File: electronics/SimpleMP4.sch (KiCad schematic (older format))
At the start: 118 parts, among them J1 USB_OTG, J2 DISPLAY, Q1 8050, Q2 SI2305, Q3 SI2305, Q4 8050, Q5 8550, Q6 SI2305, U1 OCP8020, U10 ZLED7012, U2 RK2608, U3 OCP21050TW18A, U4 OCP1240, U5 MT25QL128ABA, U6 K9HCG08U1M-PCB0/PIB0, U7 K4S641632N, U8 TRS_5PIN, U9 MMC/SD_SOCKET, Y1 24MHz

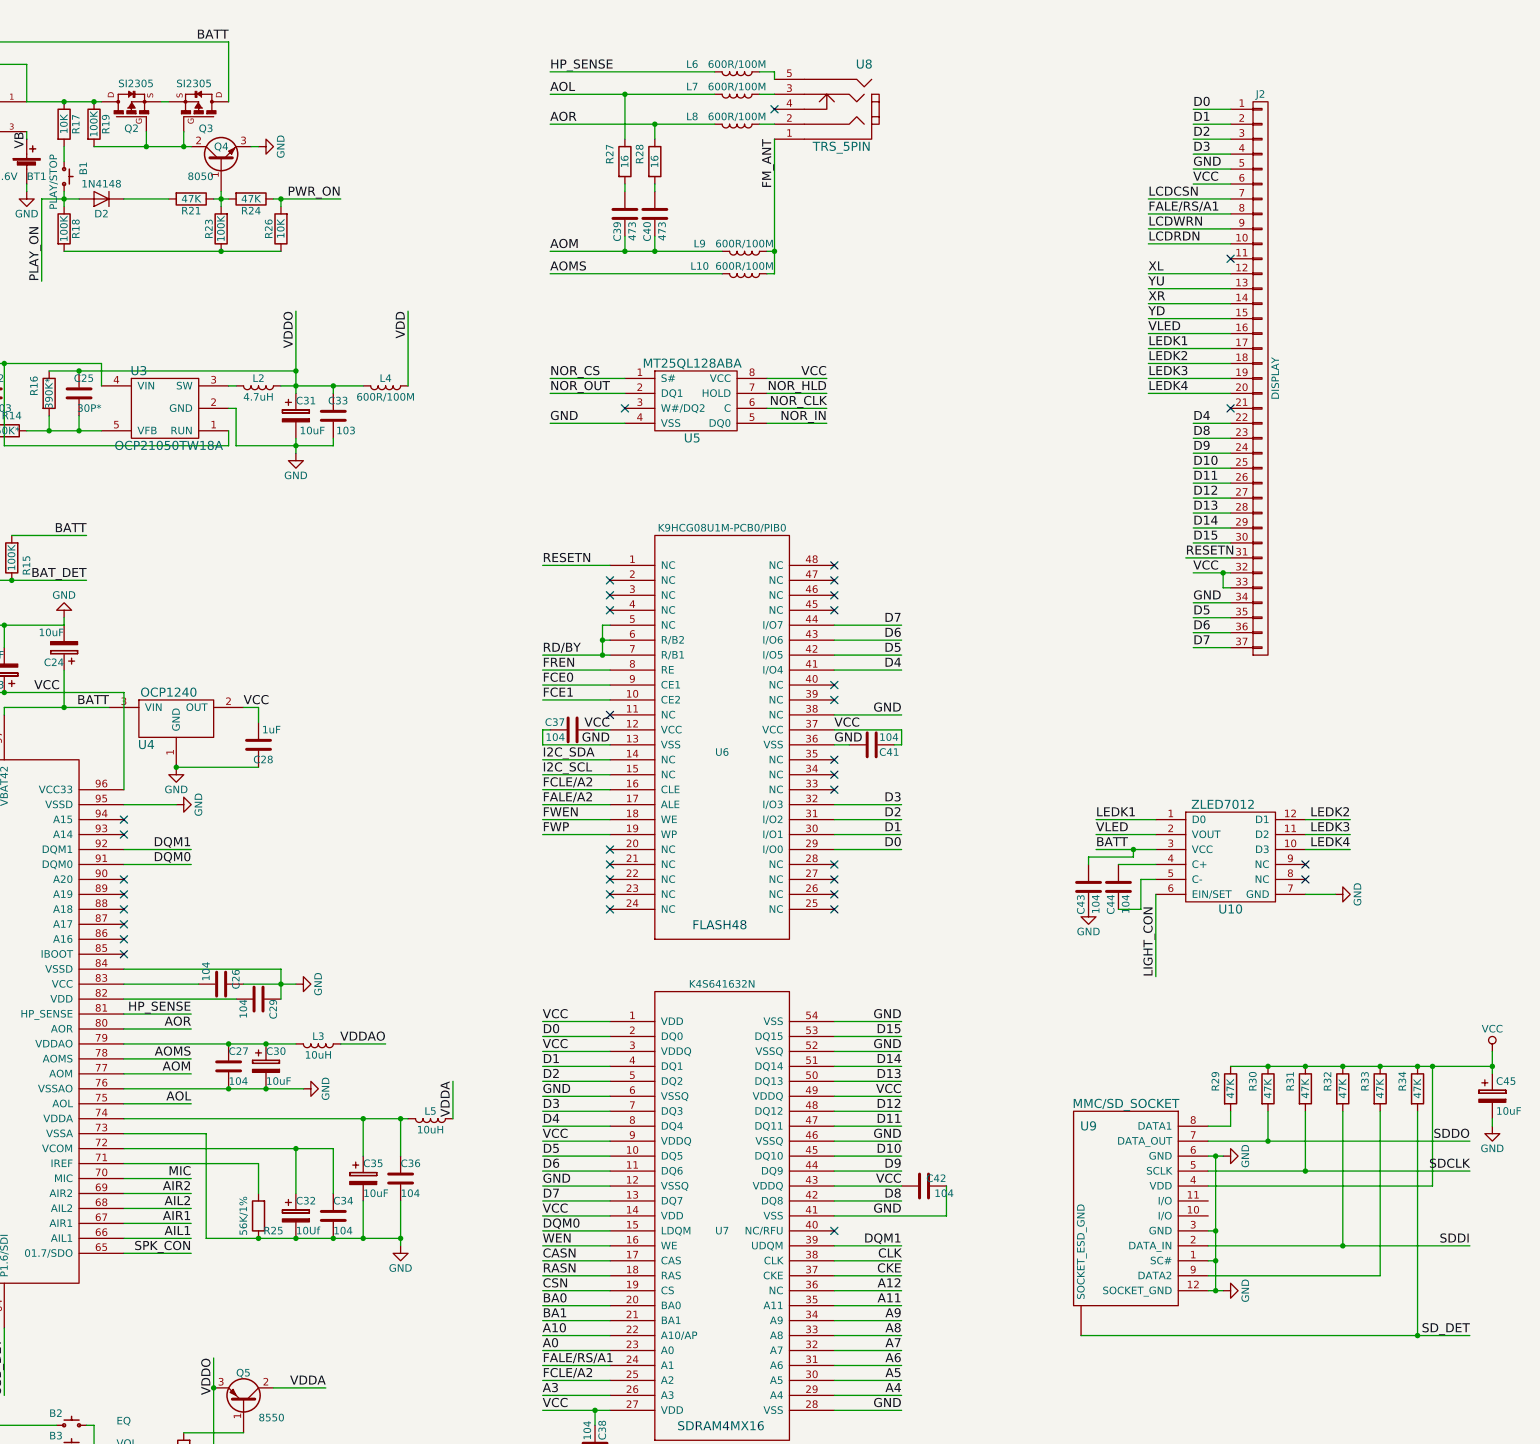
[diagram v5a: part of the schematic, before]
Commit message: cleaning up schematic
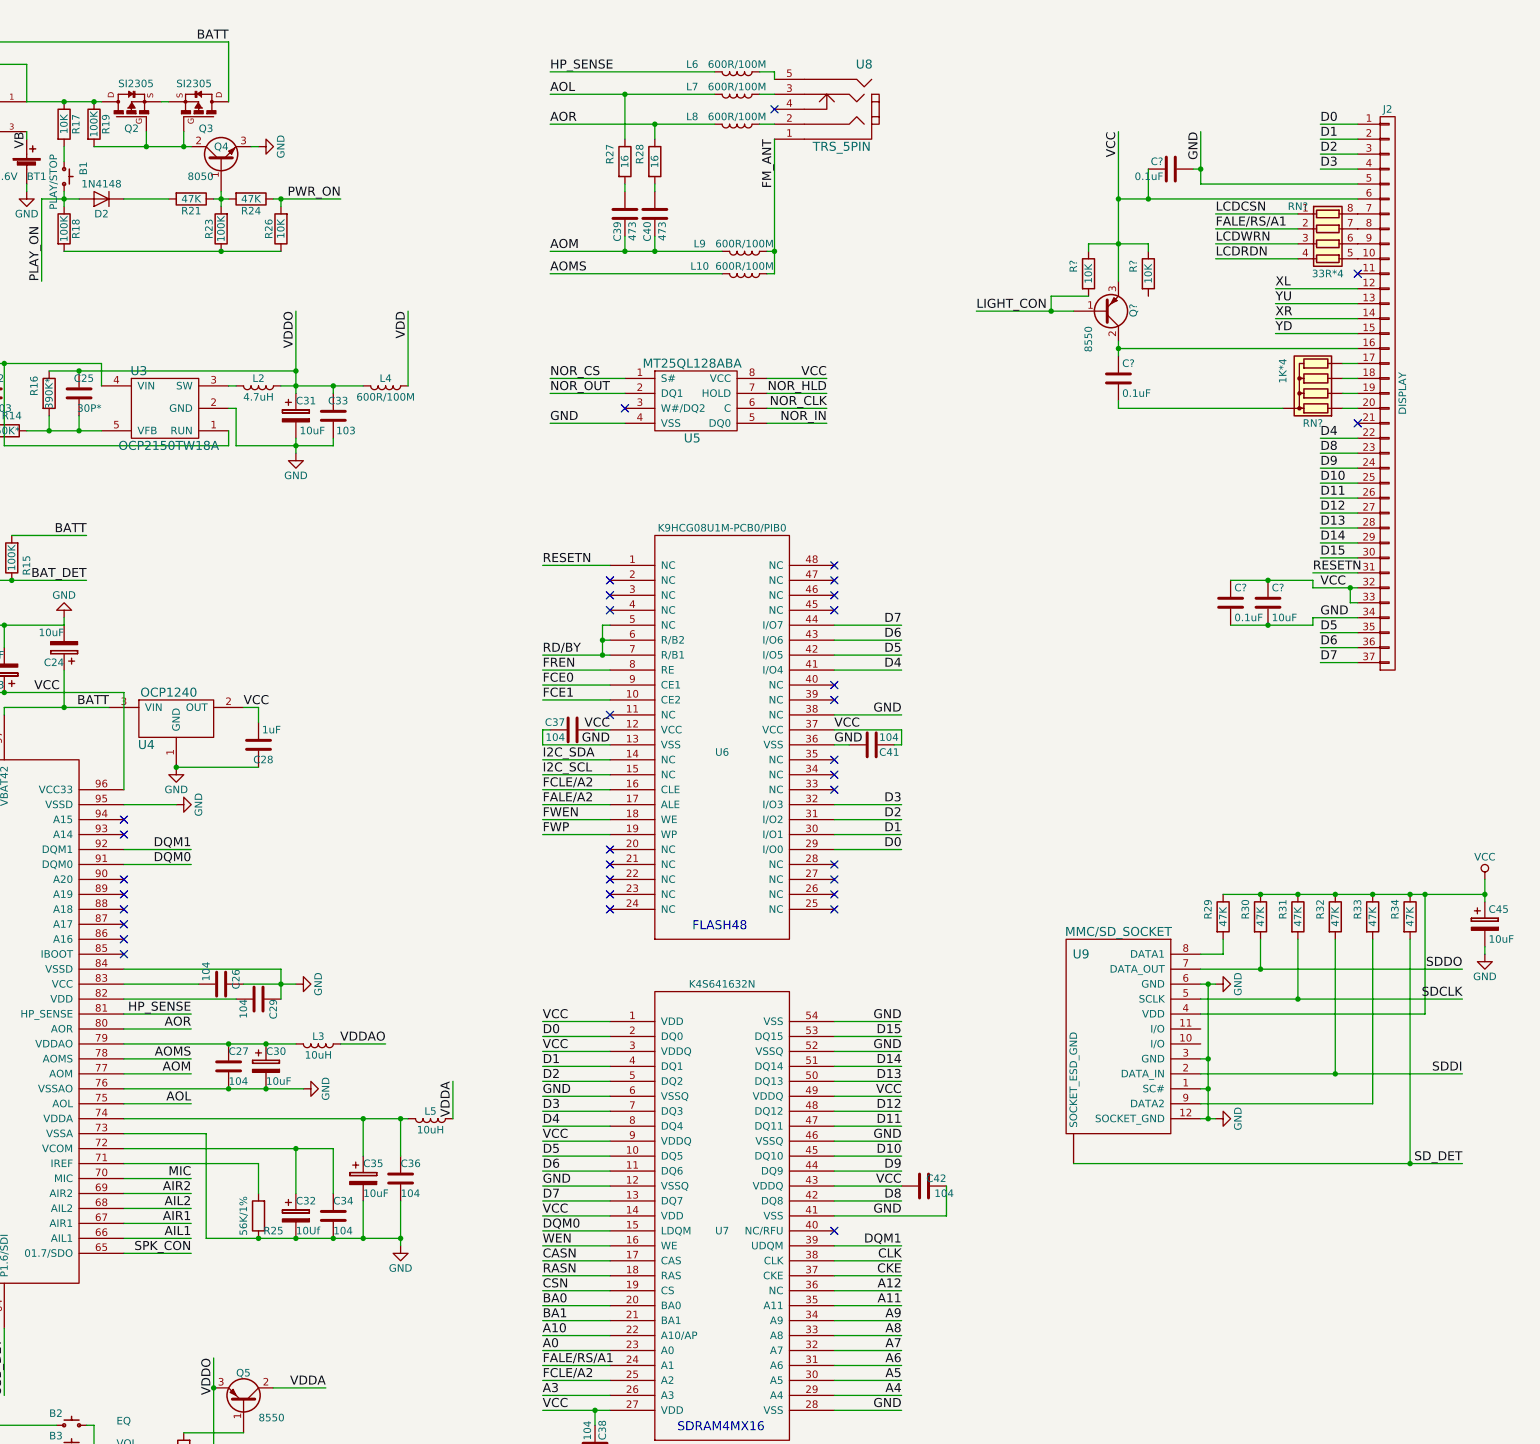
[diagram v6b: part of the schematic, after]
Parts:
- removed C43, C44: 104, symbol C
- removed U10: ZLED7012, symbol ZLED7012
- added C? (x3): 0.1uF, symbol C
- added C?: 10uF, symbol C
- added Q?: 8550, symbol Q_PNP_BCE
- added R? (x2): 10K, symbol R
- added RN?: 33R*4, symbol R_Pack04
- added RN?: 1K*4, Resistors_THT:R_Array_SIP5, symbol R_Network04
- U3: value OCP21050TW18A -> OCP2150TW18A
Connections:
- net FALE/RS/A1: now also RN?.2 (R2.1); no longer J2.8 (P8)
- net GND: now also C?.2, C?.2, C?.2
- net LCDCSN: now also RN?.1 (R1.1); no longer J2.7 (P7)
- net LCDRDN: now also RN?.4 (R4.1); no longer J2.10 (P10)
- net LCDWRN: now also RN?.3 (R3.1); no longer J2.9 (P9)
- net LIGHT_CON: now also Q?.1 (B), R?.2
- net VCC: now also C?.1, C?.1, C?.1, Q?.3 (E), R?.1, R?.1
- net LEDK1: no longer names the net of J2.17 (P17)
- net LEDK1: now also RN?.5 (R4)
- net LEDK2: no longer names the net of J2.18 (P18)
- net LEDK2: now also RN?.4 (R3)
- net LEDK3: no longer names the net of J2.19 (P19)
- net LEDK3: now also RN?.3 (R2)
- net LEDK4: no longer names the net of J2.20 (P20)
- net LEDK4: now also RN?.2 (R1)
- net VLED: no longer names the net of J2.16 (P16)
- net VLED: now also C?.1, Q?.2 (C)
- new net: J2.10 (P10), RN?.5 (R4.2)
- new net: J2.7 (P7), RN?.8 (R1.2)
- new net: J2.8 (P8), RN?.7 (R2.2)
- new net: J2.9 (P9), RN?.6 (R3.2)
- new net: C?.2, RN?.1 (common)
- no-connect marks 39 -> 37
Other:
- moved on the sheet: C45, J2, R29, R30, R31, R32, R33, R34, U9

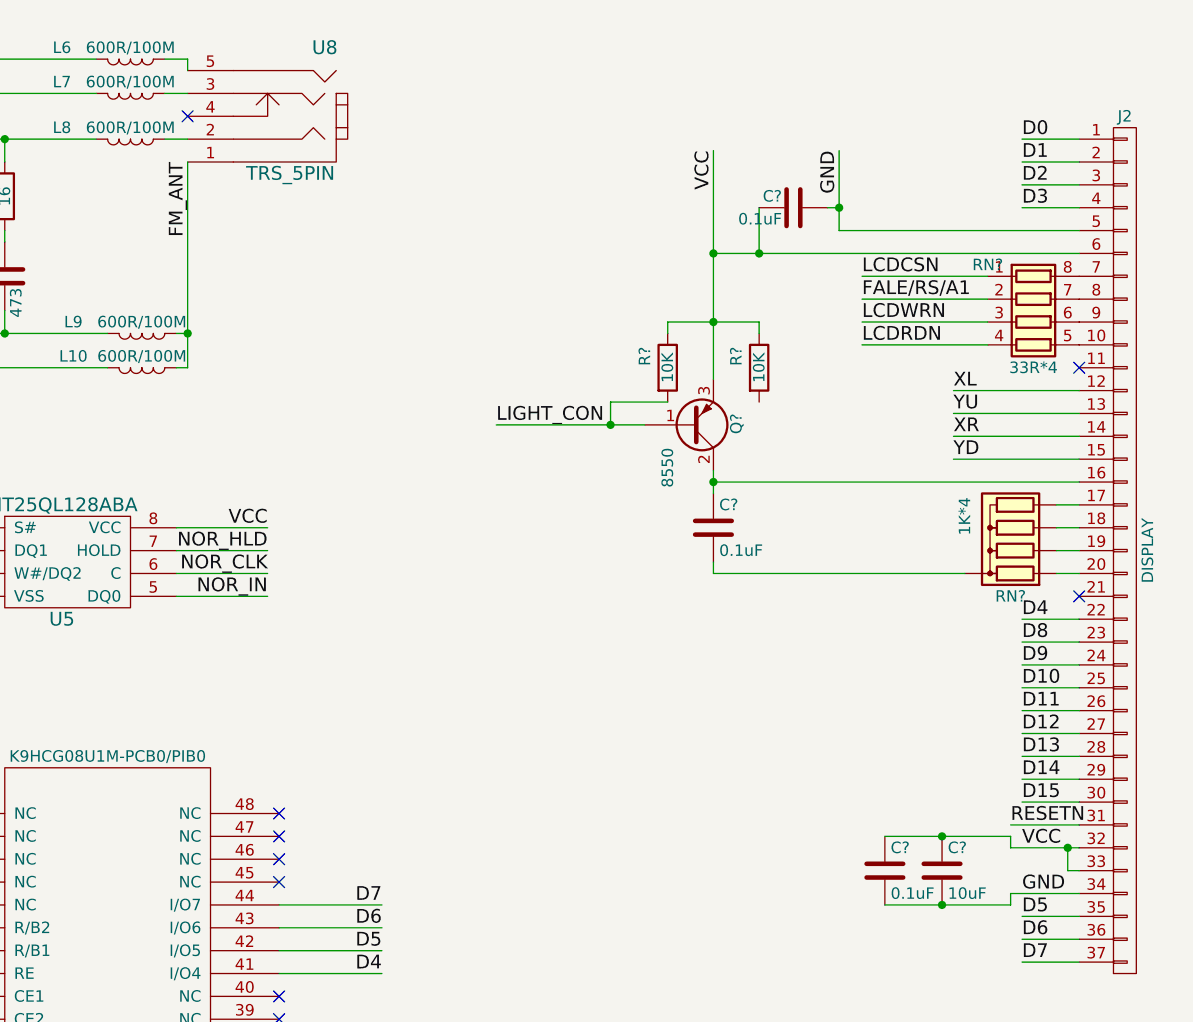
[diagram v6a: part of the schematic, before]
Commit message: added proper BOM for client
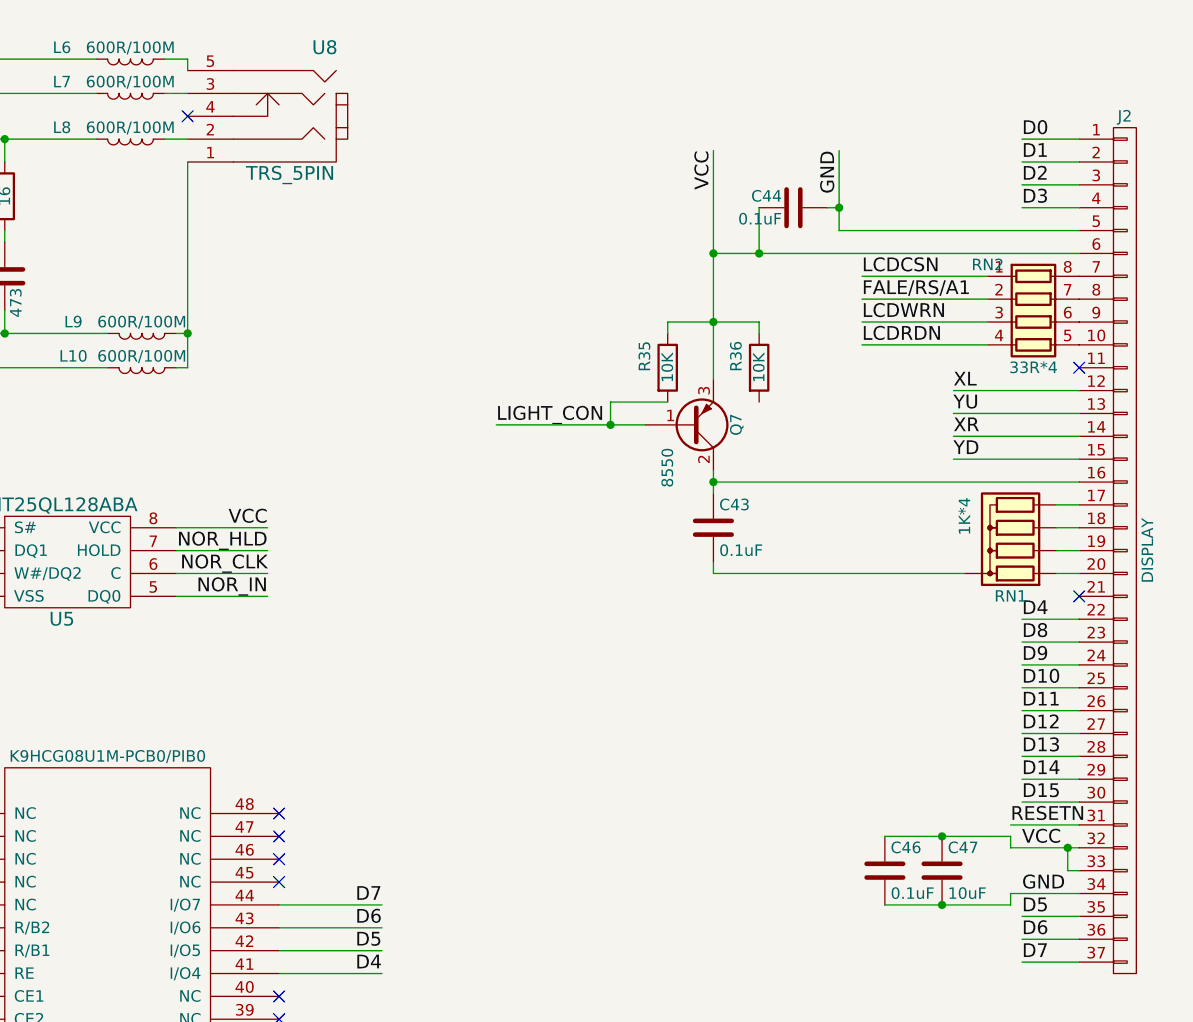
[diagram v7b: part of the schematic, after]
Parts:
- gave numbers to parts that had none: 9
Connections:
- net FM_ANT: no longer names the net of L10.1, L9.1, U8.1
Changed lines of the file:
@@
 $EndComp
 $Comp
-L GND #PWR31
+L GND #PWR30
 U 1 1 5A30ADED
 P 13700 7100
-F 0 "#PWR31" H 13700 6850 50  0001 C CNN
+F 0 "#PWR30" H 13700 6850 50  0001 C CNN
 F 1 "GND" H 13700 6950 50  0000 C CNN
 F 2 "" H 13700 7100 50  0001 C CNN
@@
 $EndComp
 $Comp
-L GND #PWR32
+L GND #PWR31
 U 1 1 5A30B9EE
 P 13700 8000
-F 0 "#PWR32" H 13700 7750 50  0001 C CNN
+F 0 "#PWR31" H 13700 7750 50  0001 C CNN
 F 1 "GND" H 13700 7850 50  0000 C CNN
 F 2 "" H 13700 8000 50  0001 C CNN
@@
 SD_DET
 $Comp
-L VCC #PWR34
+L VCC #PWR32
 U 1 1 5A30D7BC
 P 15500 6400
-F 0 "#PWR34" H 15500 6250 50  0001 C CNN
+F 0 "#PWR32" H 15500 6250 50  0001 C CNN
 F 1 "VCC" H 15500 6550 50  0000 C CNN
 F 2 "" H 15500 6400 50  0001 C CNN
@@
 $EndComp
 $Comp
-L GND #PWR35
+L GND #PWR33
 U 1 1 5A30E0B4
 P 15500 6900
-F 0 "#PWR35" H 15500 6650 50  0001 C CNN
+F 0 "#PWR33" H 15500 6650 50  0001 C CNN
 F 1 "GND" H 15500 6750 50  0000 C CNN
 F 2 "" H 15500 6900 50  0001 C CNN
@@
 AOMS
 NoConn ~ 10750 1250
-Text Label 10750 1450 3    60   ~ 0
-FM_ANT
 $Comp
 L MT25QL128ABA U5
@@
 VCC
 $Comp
-L R_Pack04 RN?
+L R_Pack04 RN2
 U 1 1 5A384FC0
 P 14450 2150
-F 0 "RN?" V 14200 1950 50  0000 C CNN
+F 0 "RN2" V 14200 1950 50  0000 C CNN
 F 1 "33R*4" V 14650 2150 50  0000 C CNN
 F 2 "" V 14725 2150 50  0001 C CNN
@@
 $EndComp
 $Comp
-L C C?
+L C C44
 U 1 1 5A38B797
 P 13400 1650
-F 0 "C?" V 13450 1700 50  0000 L CNN
+F 0 "C44" V 13450 1700 50  0000 L CNN
 F 1 "0.1uF" V 13350 1700 50  0000 L CNN
 F 2 "" H 13438 1500 50  0001 C CNN
@@
 $EndComp
 $Comp
-L R R?
+L R R35
 U 1 1 5A38C944
 P 12850 2350
-F 0 "R?" V 12750 2400 50  0000 C CNN
+F 0 "R35" V 12750 2400 50  0000 C CNN
 F 1 "10K" V 12850 2350 50  0000 C CNN
 F 2 "" V 12780 2350 50  0001 C CNN
@@
 $EndComp
 $Comp
-L R R?
+L R R36
 U 1 1 5A38CC9D
 P 13250 2350
-F 0 "R?" V 13150 2400 50  0000 C CNN
+F 0 "R36" V 13150 2400 50  0000 C CNN
 F 1 "10K" V 13250 2350 50  0000 C CNN
 F 2 "" V 13180 2350 50  0001 C CNN
@@
 $EndComp
 $Comp
-L Q_PNP_BCE Q?
+L Q_PNP_BCE Q7
 U 1 1 5A38D49C
 P 12950 2600
-F 0 "Q?" V 13150 2550 50  0000 L CNN
+F 0 "Q7" V 13150 2550 50  0000 L CNN
 F 1 "8550" V 12850 2700 50  0000 L CNN
 F 2 "" H 13150 2700 50  0001 C CNN
@@
 LIGHT_CON
 $Comp
-L R_Network04 RN?
+L R_Network04 RN1
 U 1 1 5A3915E2
 P 14350 3050
-F 0 "RN?" V 14050 3050 50  0000 C CNN
+F 0 "RN1" V 14050 3050 50  0000 C CNN
 F 1 "1K*4" H 14400 3250 50  0000 C CNN
 F 2 "Resistors_THT:R_Array_SIP5" V 14625 3050 50  0001 C CNN
@@
 $EndComp
 $Comp
-L C C?
+L C C43
 U 1 1 5A3928DF
 P 13050 3050
-F 0 "C?" H 13075 3150 50  0000 L CNN
+F 0 "C43" H 13075 3150 50  0000 L CNN
 F 1 "0.1uF" H 13075 2950 50  0000 L CNN
 F 2 "" H 13088 2900 50  0001 C CNN
@@
 $EndComp
 $Comp
-L C C?
+L C C47
 U 1 1 5A3964D5
 P 14050 4550
-F 0 "C?" H 14075 4650 50  0000 L CNN
+F 0 "C47" H 14075 4650 50  0000 L CNN
 F 1 "10uF" H 14075 4450 50  0000 L CNN
 F 2 "" H 14088 4400 50  0001 C CNN
@@
 $EndComp
 $Comp
-L C C?
+L C C46
 U 1 1 5A396667
 P 13800 4550
-F 0 "C?" H 13825 4650 50  0000 L CNN
+F 0 "C46" H 13825 4650 50  0000 L CNN
 F 1 "0.1uF" H 13825 4450 50  0000 L CNN
 F 2 "" H 13838 4400 50  0001 C CNN
